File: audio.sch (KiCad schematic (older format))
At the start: 37 parts

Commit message: use local socket & model
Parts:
- U? (x3): footprint Package_DIP:DIP-8_W7.62mm_Socket_LongPads -> stdlibmods:DIP-8_W7.62mm_Socket_LongPads
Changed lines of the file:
@@
 F 0 "U?" H 8000 2950 50  0000 C CNN
 F 1 "NJM4556A" H 8050 3200 50  0000 C CNN
-F 2 "Package_DIP:DIP-8_W7.62mm_Socket_LongPads" H 8050 2950 50  0001 C CNN
+F 2 "stdlibmods:DIP-8_W7.62mm_Socket_LongPads" H 8050 2950 50  0001 C CNN
 F 3 "https://www.te.com/commerce/DocumentDelivery/DDEController?Action=srchrtrv&DocNm=2199298&DocType=Customer+Drawing&DocLang=English" H 8050 2950 50  0001 C CNN
 F 4 "CONN IC DIP SOCKET 8POS TIN" H 0   0   50  0001 C CNN "Description"
@@
 F 0 "U?" H 5550 3000 50  0000 C CNN
 F 1 "NJM2068" H 5600 3250 50  0000 C CNN
-F 2 "Package_DIP:DIP-8_W7.62mm_Socket_LongPads" H 5600 3000 50  0001 C CNN
+F 2 "stdlibmods:DIP-8_W7.62mm_Socket_LongPads" H 5600 3000 50  0001 C CNN
 F 3 "https://www.te.com/commerce/DocumentDelivery/DDEController?Action=srchrtrv&DocNm=2199298&DocType=Customer+Drawing&DocLang=English" H 5600 3000 50  0001 C CNN
 F 4 "CONN IC DIP SOCKET 8POS TIN" H 0   0   50  0001 C CNN "Description"
@@
 F 0 "U?" H 8000 4450 50  0000 C CNN
 F 1 "NJM4556A" H 8050 4700 50  0000 C CNN
-F 2 "Package_DIP:DIP-8_W7.62mm_Socket_LongPads" H 8050 4450 50  0001 C CNN
+F 2 "stdlibmods:DIP-8_W7.62mm_Socket_LongPads" H 8050 4450 50  0001 C CNN
 F 3 "https://www.te.com/commerce/DocumentDelivery/DDEController?Action=srchrtrv&DocNm=2199298&DocType=Customer+Drawing&DocLang=English" H 8050 4450 50  0001 C CNN
 F 4 "CONN IC DIP SOCKET 8POS TIN" H 0   0   50  0001 C CNN "Description"

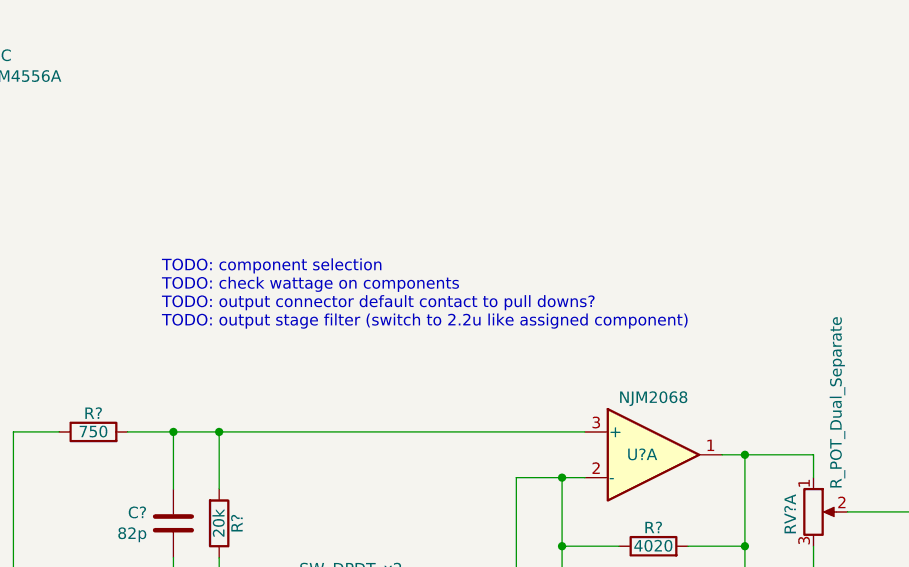
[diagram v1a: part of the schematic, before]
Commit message: add op amp components
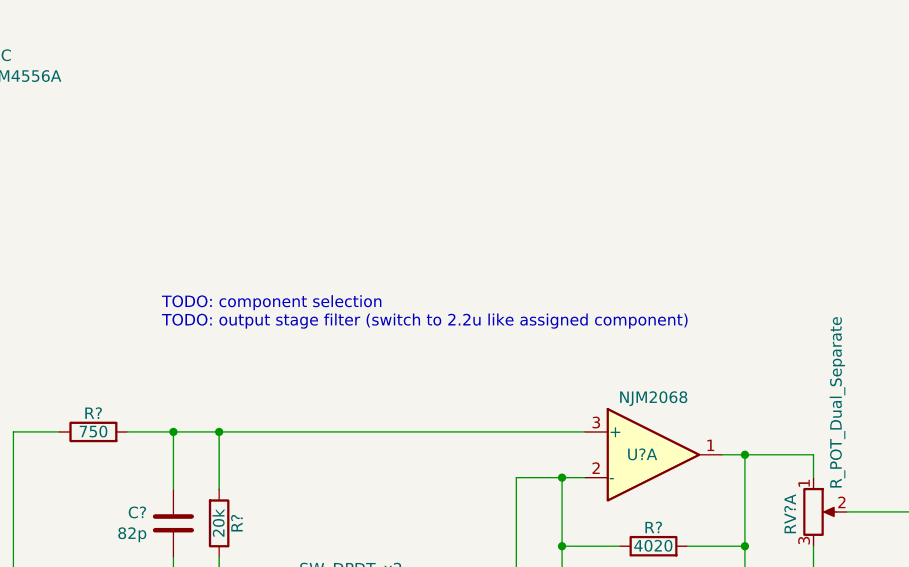
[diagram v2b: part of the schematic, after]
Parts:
- U? (x2): Description (none) -> Op Amps Dual High Current; Manufacturer (none) -> NJR; Manufacturer Part Number (none) -> NJM4556ADD; Supplier (none) -> Mouser; Supplier Part Number (none) -> 513-NJM4556ADD
- U?: footprint stdlibmods:DIP-8_W7.62mm_Socket_LongPads -> (none)
- U?: Description (none) -> Op Amps Dual Low Noise; Manufacturer (none) -> NJR; Manufacturer Part Number (none) -> NJM2068DD; Supplier (none) -> Mouser; Supplier Part Number (none) -> 513-NJM2068DD
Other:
- note added: "TODO: component selection\nTODO: output stage filter (switch to 2.2u like assigned component)"
- note removed: "TODO: component selection\nTODO: check wattage on components\nTODO: output connector default contact to pull downs?\nTODO: output stage filter (switch to 2.2u like assigned component)"
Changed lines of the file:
@@
 F 2 "" H 8050 3550 50  0001 C CNN
 F 3 "http://www.njr.com/semicon/PDF/NJM4556A_E.pdf" H 8050 3550 50  0001 C CNN
+F 4 "Op Amps Dual High Current" H 0   0   50  0001 C CNN "Description"
+F 5 "NJR" H 0   0   50  0001 C CNN "Manufacturer"
+F 6 "NJM4556ADD" H 0   0   50  0001 C CNN "Manufacturer Part Number"
+F 7 "Mouser" H 0   0   50  0001 C CNN "Supplier"
+F 8 "513-NJM4556ADD" H 0   0   50  0001 C CNN "Supplier Part Number"
 	2    8050 3550
 	1    0    0    -1
@@
 F 1 "NJM4556A" H 2158 1255 50  0000 L CNN
 F 2 "" H 2200 1300 50  0001 C CNN
-F 3 "http://www.njr.com/semicon/PDF/NJM4556A_E.pdf" H 2200 1300 50  0001 C CNN
+F 3 "" H 2200 1300 50  0001 C CNN
 	3    2200 1300
 	1    0    0    -1
@@
 F 0 "U?" H 5550 3000 50  0000 C CNN
 F 1 "NJM2068" H 5600 3250 50  0000 C CNN
-F 2 "stdlibmods:DIP-8_W7.62mm_Socket_LongPads" H 5600 3000 50  0001 C CNN
-F 3 "https://www.te.com/commerce/DocumentDelivery/DDEController?Action=srchrtrv&DocNm=2199298&DocType=Customer+Drawing&DocLang=English" H 5600 3000 50  0001 C CNN
+F 2 "" H 5600 3000 50  0001 C CNN
+F 3 "" H 5600 3000 50  0001 C CNN
 F 4 "CONN IC DIP SOCKET 8POS TIN" H 0   0   50  0001 C CNN "Description"
 F 5 "TE Connectivity AMP Connectors" H 0   0   50  0001 C CNN "Manufacturer"
@@
 F 2 "" H 5600 5000 50  0001 C CNN
 F 3 "" H 5600 5000 50  0001 C CNN
-F 4 "" H 0   0   50  0001 C CNN "Description"
-F 5 "" H 0   0   50  0001 C CNN "Manufacturer"
-F 6 "" H 0   0   50  0001 C CNN "Manufacturer Part Number"
-F 7 "" H 0   0   50  0001 C CNN "Supplier"
-F 8 "" H 0   0   50  0001 C CNN "Supplier Part Number"
+F 4 "Op Amps Dual Low Noise" H 5650 5100 50  0001 C CNN "Description"
+F 5 "NJR" H 5750 5200 50  0001 C CNN "Manufacturer"
+F 6 "NJM2068DD" H 5850 5300 50  0001 C CNN "Manufacturer Part Number"
+F 7 "Mouser" H 5950 5400 50  0001 C CNN "Supplier"
+F 8 "513-NJM2068DD" H 6050 5500 50  0001 C CNN "Supplier Part Number"
 	2    5600 5000
 	1    0    0    1
@@
 F 2 "" H 1700 1300 50  0001 C CNN
 F 3 "" H 1700 1300 50  0001 C CNN
-F 4 "" H 0   0   50  0001 C CNN "Description"
-F 5 "" H 0   0   50  0001 C CNN "Manufacturer"
-F 6 "" H 0   0   50  0001 C CNN "Manufacturer Part Number"
-F 7 "" H 0   0   50  0001 C CNN "Supplier"
-F 8 "" H 0   0   50  0001 C CNN "Supplier Part Number"
 	3    1700 1300
 	1    0    0    -1
@@
 	3700 4000 3700 4300
 Text Notes 3450 2450 0    50   ~ 0
-TODO: component selection\nTODO: check wattage on components\nTODO: output connector default contact to pull downs?\nTODO: output stage filter (switch to 2.2u like assigned component)
+TODO: component selection\nTODO: output stage filter (switch to 2.2u like assigned component)
 $Comp
 L Amplifier_Operational:NJM4556A U?
@@
 F 1 "NJM4556A" H 2658 1255 50  0000 L CNN
 F 2 "" H 2700 1300 50  0001 C CNN
-F 3 "http://www.njr.com/semicon/PDF/NJM4556A_E.pdf" H 2700 1300 50  0001 C CNN
+F 3 "" H 2700 1300 50  0001 C CNN
 	3    2700 1300
 	1    0    0    -1
@@
 F 2 "" H 8050 5050 50  0001 C CNN
 F 3 "http://www.njr.com/semicon/PDF/NJM4556A_E.pdf" H 8050 5050 50  0001 C CNN
+F 4 "Op Amps Dual High Current" H 0   0   50  0001 C CNN "Description"
+F 5 "NJR" H 0   0   50  0001 C CNN "Manufacturer"
+F 6 "NJM4556ADD" H 0   0   50  0001 C CNN "Manufacturer Part Number"
+F 7 "Mouser" H 0   0   50  0001 C CNN "Supplier"
+F 8 "513-NJM4556ADD" H 0   0   50  0001 C CNN "Supplier Part Number"
 	2    8050 5050
 	1    0    0    -1

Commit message: match audio jack to footprint
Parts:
- J? (x2): footprint (none) -> amphenol:CONN_6.35mm_Amphenol_ACJS-MHDR
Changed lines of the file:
@@
 F 0 "J?" H 2200 3700 50  0000 R CNN
 F 1 "AudioJack3_Switch" H 2150 4450 50  0000 C CNN
-F 2 "" H 2200 4100 50  0001 C CNN
+F 2 "amphenol:CONN_6.35mm_Amphenol_ACJS-MHDR" H 2200 4100 50  0001 C CNN
 F 3 "https://www.amphenol-sine.com/pdf/datasheet/ACJS-MHDR.pdf" H 2200 4100 50  0001 C CNN
 F 4 "CONN JACK STEREO 1/4\" R/A" H 0   0   50  0001 C CNN "Description"
@@
 F 0 "J?" H 9750 3700 50  0000 R CNN
 F 1 "AudioJack3_Switch" H 9700 4450 50  0000 C CNN
-F 2 "" H 9750 4100 50  0001 C CNN
+F 2 "amphenol:CONN_6.35mm_Amphenol_ACJS-MHDR" H 9750 4100 50  0001 C CNN
 F 3 "https://www.amphenol-sine.com/pdf/datasheet/ACJS-MHDR.pdf" H 9750 4100 50  0001 C CNN
 F 4 "CONN JACK STEREO 1/4\" R/A" H 200 0   50  0001 C CNN "Description"

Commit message: switch to 4.7uF WIMA caps in output stage
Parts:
- C? (x2): value 10u -> 4.7u; footprint Capacitor_THT:C_Rect_L31.5mm_W11.0mm_P27.50mm_MKS4 -> Capacitor_THT:C_Rect_L31.5mm_W15.0mm_P27.50mm_MKS4; Description CAP FILM 2.2UF 5% 250VDC RAD -> Film Capacitors 4.7uF 250 Volts 5%; Manufacturer Part Number MKP4F042206B00JSSD -> MKP4F044706F00JSSD; Supplier Digi-Key -> Mouser; Supplier Part Number 1928-1546-ND -> 505-MKP4F044706F00JS
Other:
- note removed: "TODO: component selection\nTODO: output stage filter (switch to 2.2u like assigned component)"
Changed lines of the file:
@@
 Wire Wire Line
 	3700 4000 3700 4300
-Text Notes 3450 2450 0    50   ~ 0
-TODO: component selection\nTODO: output stage filter (switch to 2.2u like assigned component)
 $Comp
 L Amplifier_Operational:NJM4556A U?
@@
 AR Path="/5CB56C16/5CEDA2A4" Ref="C?"  Part="1"
 F 0 "C?" H 6785 3204 50  0000 R CNN
-F 1 "10u" H 6785 3295 50  0000 R CNN
-F 2 "Capacitor_THT:C_Rect_L31.5mm_W11.0mm_P27.50mm_MKS4" H 6938 3100 50  0001 C CNN
-F 3 "https://www.wima.de/wp-content/uploads/media/e_WIMA_MKP_4.pdf" H 6900 3250 50  0001 C CNN
-F 4 "CAP FILM 2.2UF 5% 250VDC RAD" H 4450 -1900 50  0001 C CNN "Description"
+F 1 "4.7u" H 6785 3295 50  0000 R CNN
+F 2 "Capacitor_THT:C_Rect_L31.5mm_W15.0mm_P27.50mm_MKS4" H 6938 3100 50  0001 C CNN
+F 3 "https://www.mouser.com/datasheet/2/440/e_WIMA_MKP_4-1139861.pdf" H 6900 3250 50  0001 C CNN
+F 4 "Film Capacitors 4.7uF 250 Volts 5%" H 4450 -1900 50  0001 C CNN "Description"
 F 5 "WIMA" H 4450 -1900 50  0001 C CNN "Manufacturer"
-F 6 "MKP4F042206B00JSSD" H 4450 -1900 50  0001 C CNN "Manufacturer Part Number"
-F 7 "Digi-Key" H 4450 -1900 50  0001 C CNN "Supplier"
-F 8 "1928-1546-ND" H 4450 -1900 50  0001 C CNN "Supplier Part Number"
+F 6 "MKP4F044706F00JSSD" H 4450 -1900 50  0001 C CNN "Manufacturer Part Number"
+F 7 "Mouser" H 4450 -1900 50  0001 C CNN "Supplier"
+F 8 "505-MKP4F044706F00JS" H 4450 -1900 50  0001 C CNN "Supplier Part Number"
 	1    6900 3250
 	0    1    1    0
@@
 AR Path="/5CB56C16/5CEE5E0B" Ref="C?"  Part="1"
 F 0 "C?" H 6785 4704 50  0000 R CNN
-F 1 "10u" H 6785 4795 50  0000 R CNN
-F 2 "Capacitor_THT:C_Rect_L31.5mm_W11.0mm_P27.50mm_MKS4" H 6938 4600 50  0001 C CNN
-F 3 "https://www.wima.de/wp-content/uploads/media/e_WIMA_MKP_4.pdf" H 6900 4750 50  0001 C CNN
-F 4 "CAP FILM 2.2UF 5% 250VDC RAD" H 4450 -400 50  0001 C CNN "Description"
+F 1 "4.7u" H 6785 4795 50  0000 R CNN
+F 2 "Capacitor_THT:C_Rect_L31.5mm_W15.0mm_P27.50mm_MKS4" H 6938 4600 50  0001 C CNN
+F 3 "https://www.mouser.com/datasheet/2/440/e_WIMA_MKP_4-1139861.pdf" H 6900 4750 50  0001 C CNN
+F 4 "Film Capacitors 4.7uF 250 Volts 5%" H 4450 -400 50  0001 C CNN "Description"
 F 5 "WIMA" H 4450 -400 50  0001 C CNN "Manufacturer"
-F 6 "MKP4F042206B00JSSD" H 4450 -400 50  0001 C CNN "Manufacturer Part Number"
-F 7 "Digi-Key" H 4450 -400 50  0001 C CNN "Supplier"
-F 8 "1928-1546-ND" H 4450 -400 50  0001 C CNN "Supplier Part Number"
+F 6 "MKP4F044706F00JSSD" H 4450 -400 50  0001 C CNN "Manufacturer Part Number"
+F 7 "Mouser" H 4450 -400 50  0001 C CNN "Supplier"
+F 8 "505-MKP4F044706F00JS" H 4450 -400 50  0001 C CNN "Supplier Part Number"
 	1    6900 4750
 	0    1    -1   0

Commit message: add missing NJM2068 BOM data
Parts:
- U?: footprint (none) -> stdlibmods:DIP-8_W7.62mm_Socket_LongPads
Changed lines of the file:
@@
 F 0 "U?" H 5550 3000 50  0000 C CNN
 F 1 "NJM2068" H 5600 3250 50  0000 C CNN
-F 2 "" H 5600 3000 50  0001 C CNN
-F 3 "" H 5600 3000 50  0001 C CNN
+F 2 "stdlibmods:DIP-8_W7.62mm_Socket_LongPads" H 5600 3000 50  0001 C CNN
+F 3 "https://www.te.com/commerce/DocumentDelivery/DDEController?Action=srchrtrv&DocNm=2199298&DocType=Customer+Drawing&DocLang=English" H 5600 3000 50  0001 C CNN
 F 4 "CONN IC DIP SOCKET 8POS TIN" H 0   0   50  0001 C CNN "Description"
 F 5 "TE Connectivity AMP Connectors" H 0   0   50  0001 C CNN "Manufacturer"
@@
 F 1 "NJM2068" H 5600 5250 50  0000 C CNN
 F 2 "" H 5600 5000 50  0001 C CNN
-F 3 "" H 5600 5000 50  0001 C CNN
+F 3 "https://www.mouser.com/datasheet/2/294/NJM2068_E-364244.pdf" H 5600 5000 50  0001 C CNN
 F 4 "Op Amps Dual Low Noise" H 5650 5100 50  0001 C CNN "Description"
 F 5 "NJR" H 5750 5200 50  0001 C CNN "Manufacturer"

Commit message: swap output stage highpass resistors to 40.2k
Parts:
- R? (x2): value 20k -> 40.2k; Description RES SMD 20K OHM 0.1% 1/8W 0805 Metal Film -> RES SMD 40.2K OHM 0.1% 1/8W 0805 Metal Film; Manufacturer Part Number ERA-6AEB203V -> ERA-6AEB4022V; Supplier Part Number P20KDACT-ND -> P40.2KDACT-ND
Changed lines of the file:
@@
 AR Path="/5CB56C16/5CEDAB07" Ref="R?"  Part="1"
 F 0 "R?" V 7430 3550 50  0000 C CNN
-F 1 "20k" V 7350 3550 50  0000 C CNN
+F 1 "40.2k" V 7350 3550 50  0000 C CNN
 F 2 "Resistor_SMD:R_0805_2012Metric_Pad1.15x1.40mm_HandSolder" V 7280 3550 50  0001 C CNN
 F 3 "https://industrial.panasonic.com/cdbs/www-data/pdf/RDM0000/AOA0000C307.pdf" H 7350 3550 50  0001 C CNN
-F 4 "RES SMD 20K OHM 0.1% 1/8W 0805 Metal Film" H 7350 3550 50  0001 C CNN "Description"
+F 4 "RES SMD 40.2K OHM 0.1% 1/8W 0805 Metal Film" H 7350 3550 50  0001 C CNN "Description"
 F 5 "Panasonic Electronic Components" H 7350 3550 50  0001 C CNN "Manufacturer"
-F 6 "ERA-6AEB203V" H 7350 3550 50  0001 C CNN "Manufacturer Part Number"
+F 6 "ERA-6AEB4022V" H 7350 3550 50  0001 C CNN "Manufacturer Part Number"
 F 7 "Digi-Key" H 7350 3550 50  0001 C CNN "Supplier"
-F 8 "P20KDACT-ND" H 7350 3550 50  0001 C CNN "Supplier Part Number"
+F 8 "P40.2KDACT-ND" H 7350 3550 50  0001 C CNN "Supplier Part Number"
 	1    7350 3550
 	-1   0    0    -1
@@
 AR Path="/5CB56C16/5CEE5E17" Ref="R?"  Part="1"
 F 0 "R?" V 7430 4450 50  0000 C CNN
-F 1 "20k" V 7350 4450 50  0000 C CNN
+F 1 "40.2k" V 7350 4450 50  0000 C CNN
 F 2 "Resistor_SMD:R_0805_2012Metric_Pad1.15x1.40mm_HandSolder" V 7280 4450 50  0001 C CNN
 F 3 "https://industrial.panasonic.com/cdbs/www-data/pdf/RDM0000/AOA0000C307.pdf" H 7350 4450 50  0001 C CNN
-F 4 "RES SMD 20K OHM 0.1% 1/8W 0805 Metal Film" H 7350 4450 50  0001 C CNN "Description"
+F 4 "RES SMD 40.2K OHM 0.1% 1/8W 0805 Metal Film" H 7350 4450 50  0001 C CNN "Description"
 F 5 "Panasonic Electronic Components" H 7350 4450 50  0001 C CNN "Manufacturer"
-F 6 "ERA-6AEB203V" H 7350 4450 50  0001 C CNN "Manufacturer Part Number"
+F 6 "ERA-6AEB4022V" H 7350 4450 50  0001 C CNN "Manufacturer Part Number"
 F 7 "Digi-Key" H 7350 4450 50  0001 C CNN "Supplier"
-F 8 "P20KDACT-ND" H 7350 4450 50  0001 C CNN "Supplier Part Number"
+F 8 "P40.2KDACT-ND" H 7350 4450 50  0001 C CNN "Supplier Part Number"
 	1    7350 4450
 	-1   0    0    1

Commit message: switch components supplier to Mouser for price/availability
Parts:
- J? (x2): Supplier Digi-Key -> Mouser; Supplier Part Number 889-1817-ND -> 523-ACJS-MHDR
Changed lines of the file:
@@
 F 5 "Amphenol Sine Systems Corp" H 0   0   50  0001 C CNN "Manufacturer"
 F 6 "ACJS-MHDR" H 0   0   50  0001 C CNN "Manufacturer Part Number"
-F 7 "Digi-Key" H 0   0   50  0001 C CNN "Supplier"
-F 8 "889-1817-ND" H 0   0   50  0001 C CNN "Supplier Part Number"
+F 7 "Mouser" H 0   0   50  0001 C CNN "Supplier"
+F 8 "523-ACJS-MHDR" H 0   0   50  0001 C CNN "Supplier Part Number"
 	1    2200 4100
 	1    0    0    1
@@
 F 5 "Amphenol Sine Systems Corp" H 200 0   50  0001 C CNN "Manufacturer"
 F 6 "ACJS-MHDR" H 200 0   50  0001 C CNN "Manufacturer Part Number"
-F 7 "Digi-Key" H 200 0   50  0001 C CNN "Supplier"
-F 8 "889-1817-ND" H 200 0   50  0001 C CNN "Supplier Part Number"
+F 7 "Mouser" H 200 0   50  0001 C CNN "Supplier"
+F 8 "523-ACJS-MHDR" H 200 0   50  0001 C CNN "Supplier Part Number"
 	1    9750 4100
 	-1   0    0    1

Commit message: add audio pot components & model
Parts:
- RV?: footprint (none) -> stdlibmods:Potentiometer_PTD902-1015K-A502; Description (none) -> Potentiometer 2 Gang Audio Taper 5kOhms; Manufacturer (none) -> Bourns; Manufacturer Part Number (none) -> PTD902-1015K-A502; Supplier (none) -> Mouser; Supplier Part Number (none) -> 652-PTD9021015KA502
- RV?: Description (none) -> KNOB KNURLED 0.236\" METAL; Manufacturer (none) -> SparkFun Electronics; Manufacturer Part Number (none) -> COM-10002; Supplier (none) -> Digi-Key; Supplier Part Number (none) -> 1568-1601-ND
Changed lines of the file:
@@
 F 0 "RV?" V 6200 3150 50  0000 L CNN
 F 1 "R_POT_Dual_Separate" V 6400 3350 50  0000 L CNN
-F 2 "" H 6300 3250 50  0001 C CNN
-F 3 "~" H 6300 3250 50  0001 C CNN
+F 2 "stdlibmods:Potentiometer_PTD902-1015K-A502" H 6300 3250 50  0001 C CNN
+F 3 "https://www.bourns.com/docs/product-datasheets/PTD90.pdf" H 6300 3250 50  0001 C CNN
+F 4 "Potentiometer 2 Gang Audio Taper 5kOhms" H 0   0   50  0001 C CNN "Description"
+F 5 "Bourns" H 0   0   50  0001 C CNN "Manufacturer"
+F 6 "PTD902-1015K-A502" H 0   0   50  0001 C CNN "Manufacturer Part Number"
+F 7 "Mouser" H 0   0   50  0001 C CNN "Supplier"
+F 8 "652-PTD9021015KA502" H 0   0   50  0001 C CNN "Supplier Part Number"
 	1    6300 3250
 	1    0    0    -1
@@
 F 1 "R_POT_Dual_Separate" V 6400 4850 50  0000 L CNN
 F 2 "" H 6300 4750 50  0001 C CNN
-F 3 "~" H 6300 4750 50  0001 C CNN
+F 3 "https://www.digikey.com/product-detail/en/sparkfun-electronics/COM-10002/1568-1601-ND/7229871" H 6300 4750 50  0001 C CNN
+F 4 "KNOB KNURLED 0.236\" METAL" H 0   0   50  0001 C CNN "Description"
+F 5 "SparkFun Electronics" H 0   0   50  0001 C CNN "Manufacturer"
+F 6 "COM-10002" H 0   0   50  0001 C CNN "Manufacturer Part Number"
+F 7 "Digi-Key" H 0   0   50  0001 C CNN "Supplier"
+F 8 "1568-1601-ND" H 0   0   50  0001 C CNN "Supplier Part Number"
 	2    6300 4750
 	1    0    0    1
